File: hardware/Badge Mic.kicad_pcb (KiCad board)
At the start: 4 copper layers, 76.2 x 27.1 mm, 38 parts, among them J1 UART, J2 Badge, SW1 SW_SPDT_MSM, SW2 SW_SPDT_MSM, U1 74HC86, U2 4081, U3 MAX9814, U4 74CBTLV3257, U5 74CBTLV3257, U6 AD7822BRUZ, U7 74HC573PW,118, U8 MAX1595EUA33+T, U9 LMV321

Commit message: Minor layout change
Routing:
- net +3V3: vias 20 -> 11
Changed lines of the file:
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@@
   (segment (start 176.64 123.66) (end 177.85 122.45) (width 0.25) (layer "B.Cu") (net 6))
   (segment (start 178.5325 122.45) (end 177.85 122.45) (width 0.25) (layer "B.Cu") (net 6))
-  (via (at 149.84 118.55) (size 0.508) (drill 0.254) (layers "F.Cu" "B.Cu") (free) (net 7))
-  (via (at 150.35 118.55) (size 0.508) (drill 0.254) (layers "F.Cu" "B.Cu") (free) (net 7))
-  (via (at 150.86 118.55) (size 0.508) (drill 0.254) (layers "F.Cu" "B.Cu") (free) (net 7))
   (via (at 175.057501 120.982496) (size 0.508) (drill 0.254) (layers "F.Cu" "B.Cu") (net 7))
   (via (at 178.94 111.63) (size 0.508) (drill 0.254) (layers "F.Cu" "B.Cu") (net 7))
@@
   (via (at 174.325 104.475) (size 0.508) (drill 0.254) (layers "F.Cu" "B.Cu") (net 7))
   (via (at 150.78179 115.629618) (size 0.508) (drill 0.254) (layers "F.Cu" "B.Cu") (net 7))
-  (via (at 149.84 118.04) (size 0.508) (drill 0.254) (layers "F.Cu" "B.Cu") (free) (net 7))
-  (via (at 149.84 119.06) (size 0.508) (drill 0.254) (layers "F.Cu" "B.Cu") (free) (net 7))
   (via (at 137.090355 108.283559) (size 0.508) (drill 0.254) (layers "F.Cu" "B.Cu") (net 7))
-  (via (at 150.86 118.04) (size 0.508) (drill 0.254) (layers "F.Cu" "B.Cu") (free) (net 7))
   (via (at 135.740355 108.383559) (size 0.508) (drill 0.254) (layers "F.Cu" "B.Cu") (net 7))
-  (via (at 150.86 119.06) (size 0.508) (drill 0.254) (layers "F.Cu" "B.Cu") (free) (net 7))
   (via (at 162.525 114.175) (size 0.508) (drill 0.254) (layers "F.Cu" "B.Cu") (net 7))
-  (via (at 150.35 118.04) (size 0.508) (drill 0.254) (layers "F.Cu" "B.Cu") (free) (net 7))
-  (via (at 150.35 119.06) (size 0.508) (drill 0.254) (layers "F.Cu" "B.Cu") (free) (net 7))
   (via (at 174.3325 103.25) (size 0.508) (drill 0.254) (layers "F.Cu" "B.Cu") (net 7))
   (via (at 163.9 114.1675) (size 0.508) (drill 0.254) (layers "F.Cu" "B.Cu") (net 7))

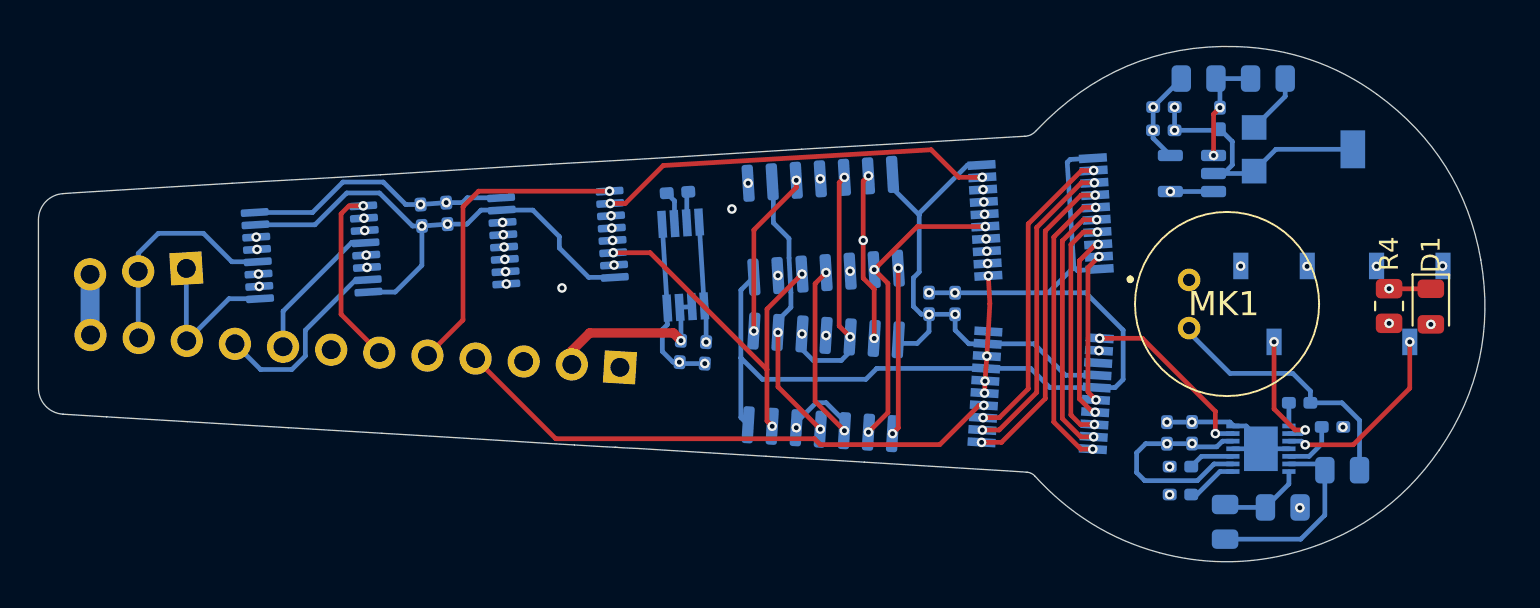
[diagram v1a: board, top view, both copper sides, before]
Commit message: Fixed DRC errors
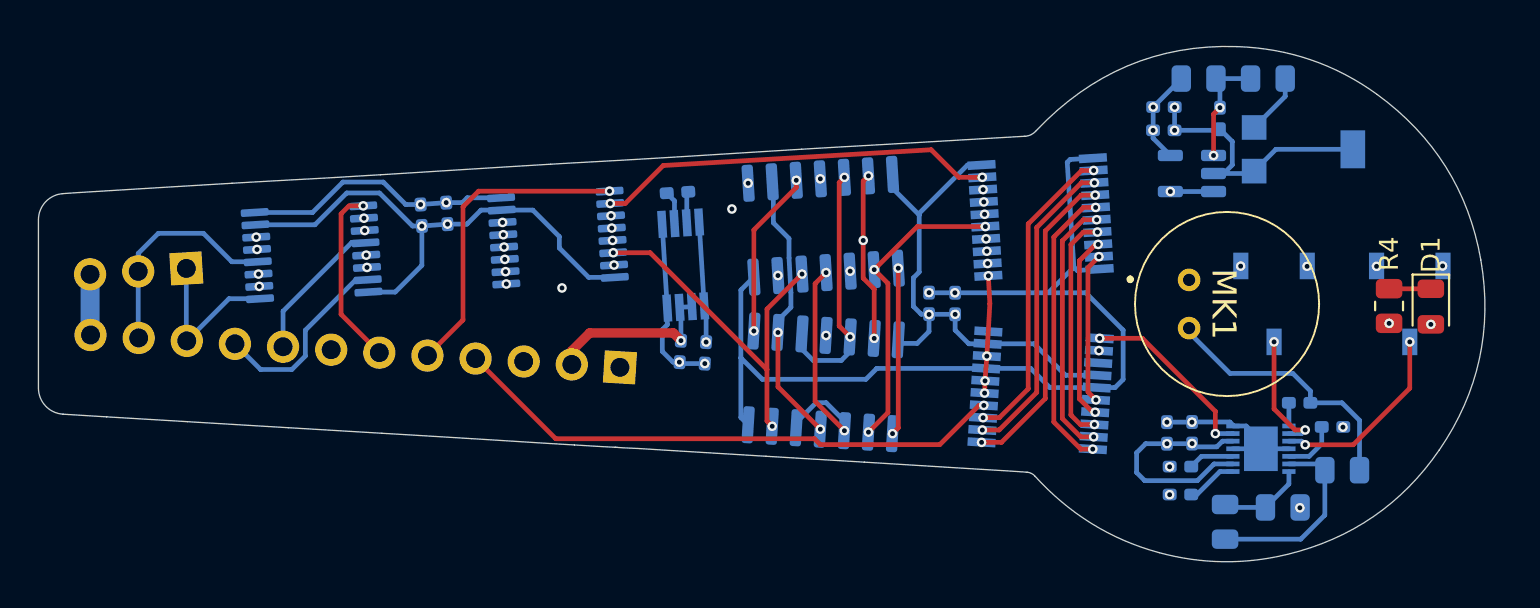
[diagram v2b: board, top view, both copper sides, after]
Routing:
- net Q5: track 40.4 -> 39.7 mm
- net Q6: track 42.0 -> 41.4 mm
- net Net-(U1-Pad4): vias 3 -> 2
- net Net-(U1-Pad12): vias 3 -> 2
- net Net-(D1-Pad1): vias 1 -> 0

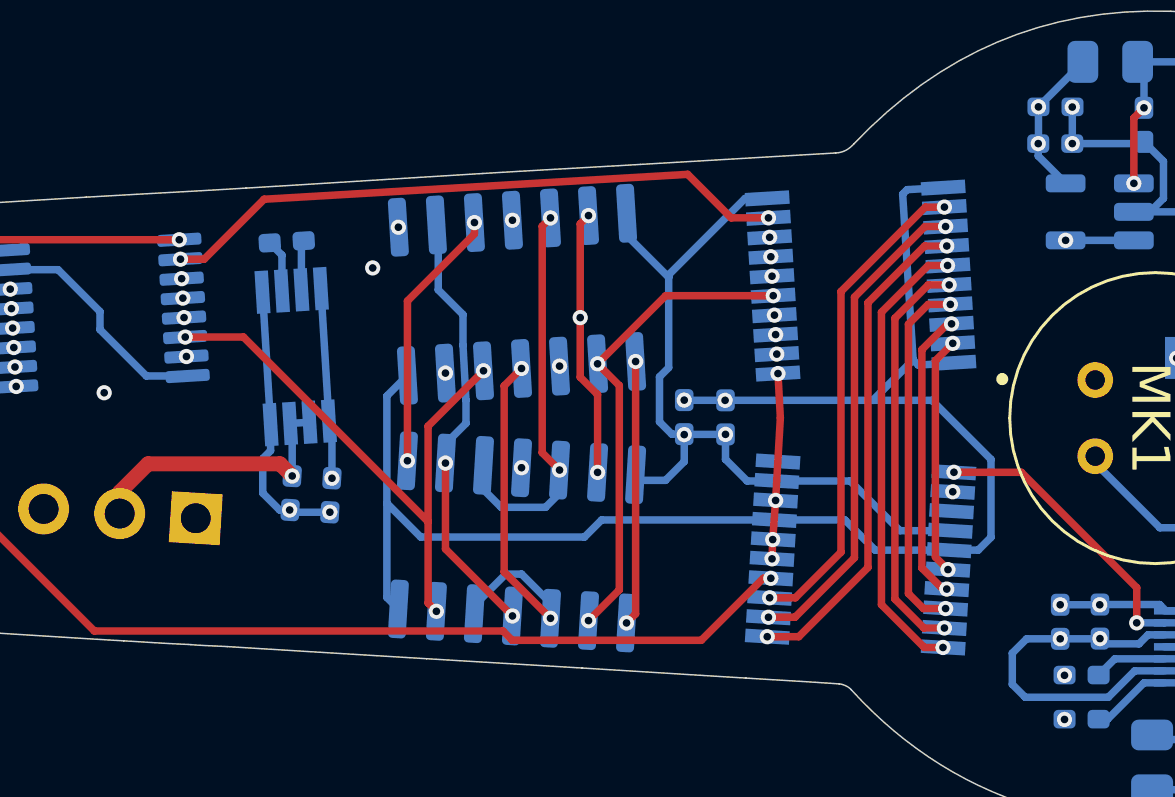
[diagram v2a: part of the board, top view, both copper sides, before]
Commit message: Improved power routing
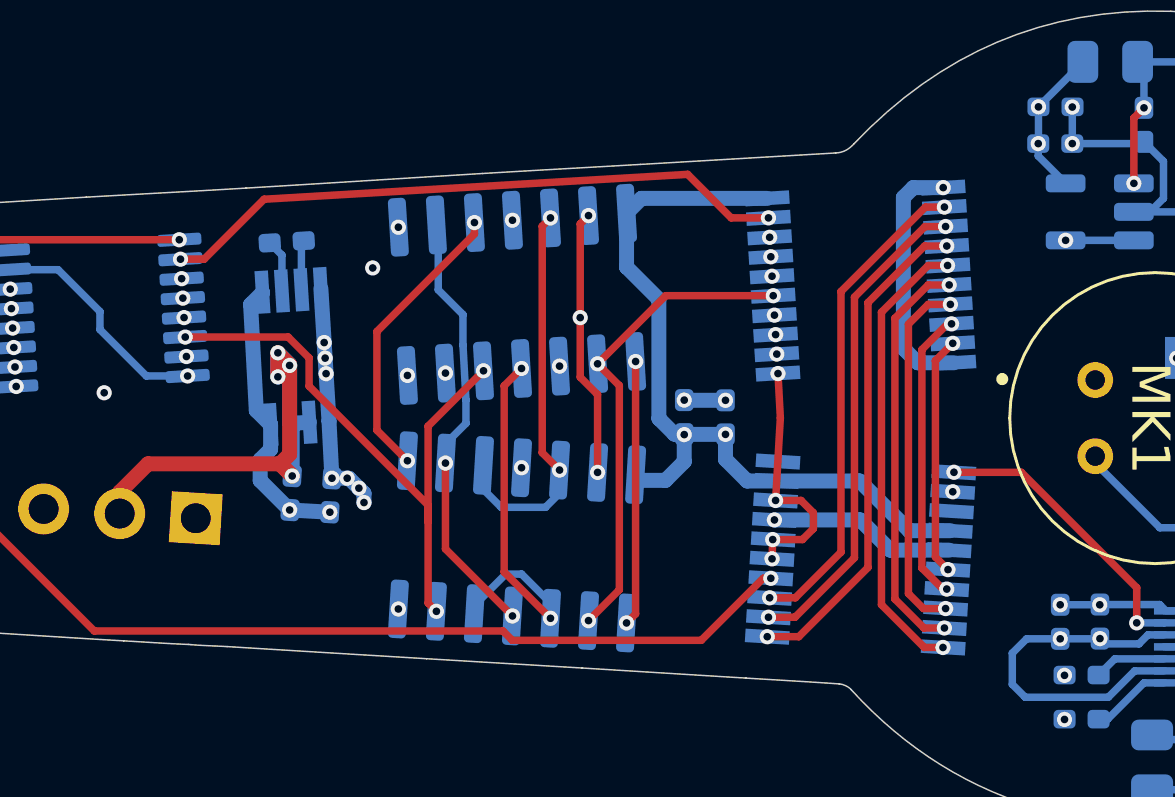
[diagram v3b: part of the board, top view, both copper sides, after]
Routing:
- net GND: track 117.6 -> 80.3 mm, vias 17 -> 22
- net VDD: track 9.45 -> 18.6 mm, vias 1 -> 4
- net EOC: track 6.19 -> 8.35 mm
- net +3V3: track 64.4 -> 66.3 mm, vias 11 -> 17
- net Net-(U1-Pad8): track 30.9 -> 32.0 mm
- net Net-(D1-Pad2): track 34.2 -> 35.2 mm
- net Q5: track 39.7 -> 40.5 mm
- net Q6: track 41.4 -> 42.2 mm

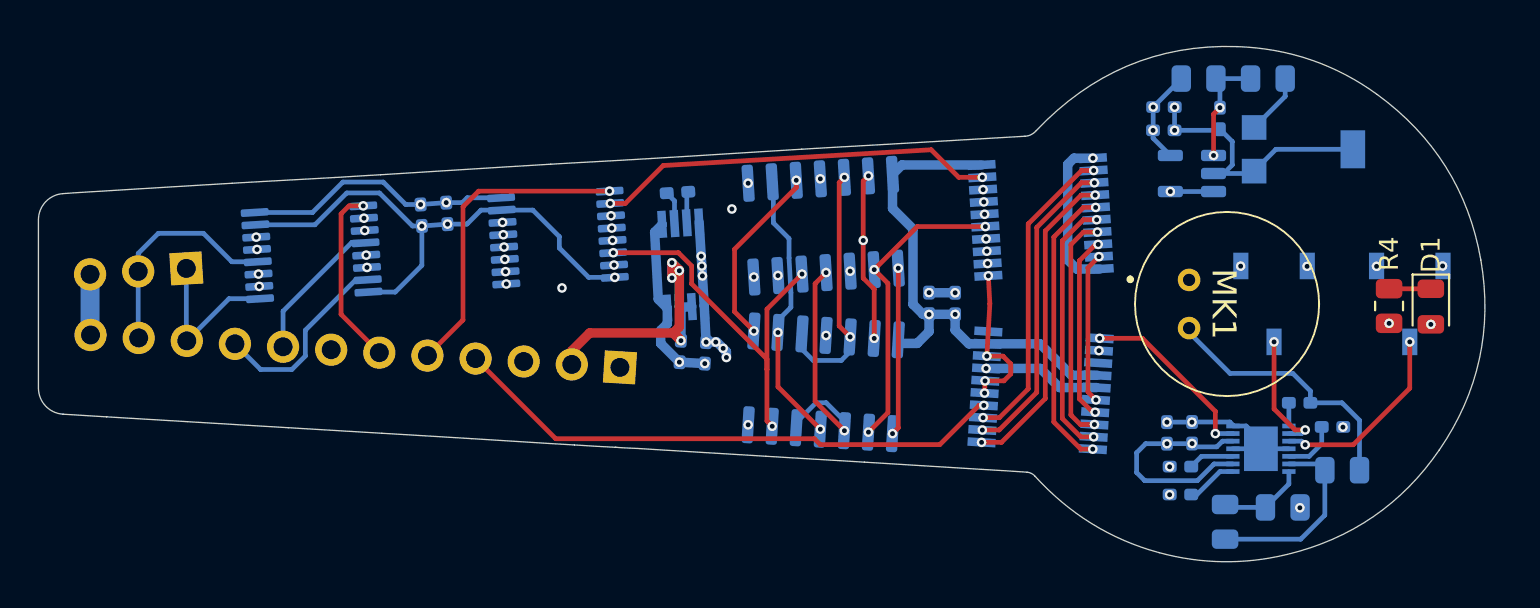
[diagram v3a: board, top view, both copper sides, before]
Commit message: Routing improvements and some silkscreen art
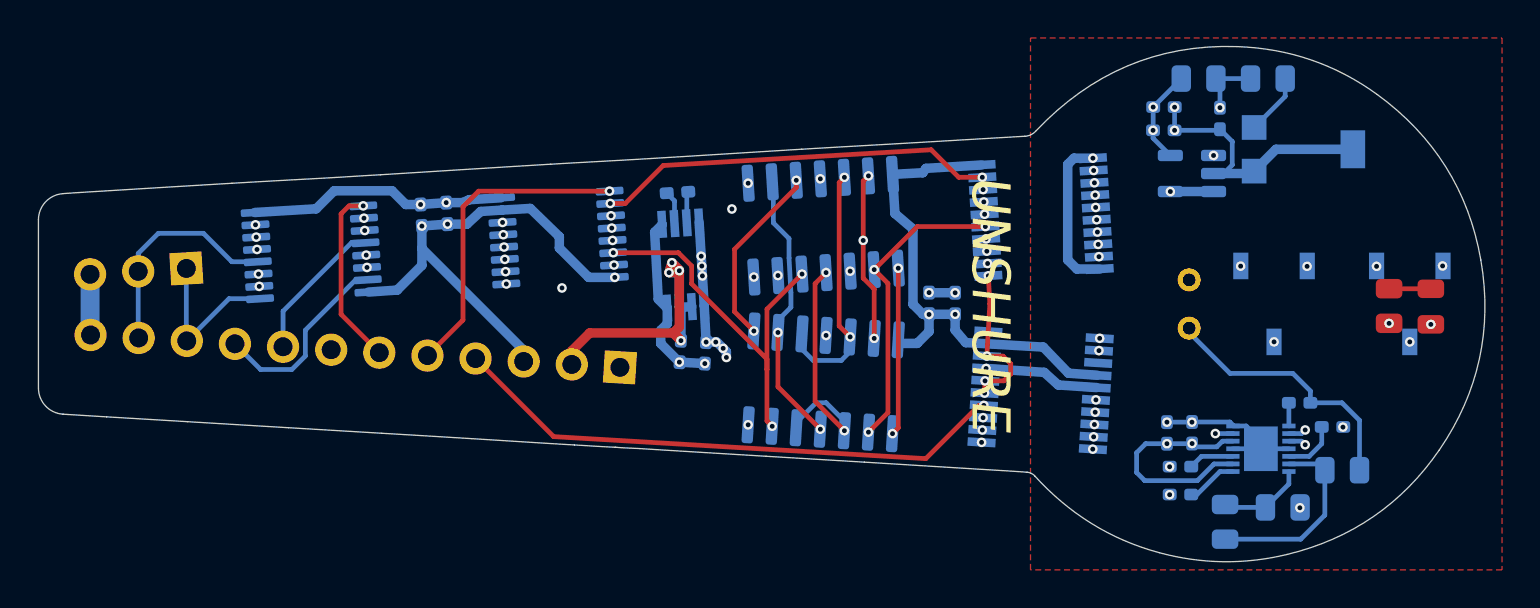
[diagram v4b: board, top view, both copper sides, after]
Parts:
- added MK1: Microphone, SamacSys_Parts:CMA6542PF, F.Cu at (176.2, 112.4)
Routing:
- net GND: track 80.3 -> 78.0 mm, vias 22 -> 23
- net +3V3: track 66.3 -> 65.4 mm
- added copper zone on F.Cu, net GND
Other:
- board text added: "2000"
- board text added: "2022"
- board text added: "40"
- board text added: "4000"
- board text added: "50"
- board text added: "500"
- board text added: "60"
- board text added: "UNSHURE"
- board text added: "adam sam and sara"
- board text added: "attack:release (1:x)"
- board text added: "center level"
- board text added: "max gain (db)"
- board text added: "supercon6"
